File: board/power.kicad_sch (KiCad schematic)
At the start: 0 parts

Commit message: add: Hierarchical Sheets
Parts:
- added C10, C11: 100n, Capacitor_SMD:C_0603_1608Metric, symbol Device:C
- added C12, C13, C14, C15: 100pF, Capacitor_SMD:C_0201_0603Metric, symbol Device:C
- added J1: UART, Connector_PinSocket_2.54mm:PinSocket_1x02_P2.54mm_Vertical, symbol Connector_Generic:Conn_01x02
- added J2: USB_B, Connector_USB:USB_Mini-B_Lumberg_2486_01_Horizontal, symbol Connector:USB_B
- added U6: FT232RL, Package_SO:SSOP-28_5.3x10.2mm_P0.65mm, symbol Interface_USB:FT232RL
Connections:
- new net: J1.1 (Pin_1), U6.1 (TXD)
- new net: J1.2 (Pin_2), U6.5 (RXD)
- new net 5V: C10.1, C11.1, C12.1, C13.1, C14.1, C15.1, J2.1 (VBUS), U6.20 (VCC), U6.4 (VCCIO)
- new net ALARM: U6.19 (~{RESET})
- new net DT+: J2.3 (D+), U6.15 (USBD+)
- new net DT-: J2.2 (D-), U6.16 (USBD-)
- new net GND: C10.2, C11.2, C12.2, C13.2, C14.2, C15.2, J2.4 (GND), J2.5 (Shield), U6.18 (GND), U6.21 (GND), U6.25 (AGND), U6.26 (TEST), U6.7 (GND)
- no-connect marks 0 -> 14
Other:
- note added: "USB_P USB_N"
- note added: "desc: provide shortest return current path"
- note added: "entry source"
- note added: "exit sink"
- note added: "plane split"
- note added: "split boundary"

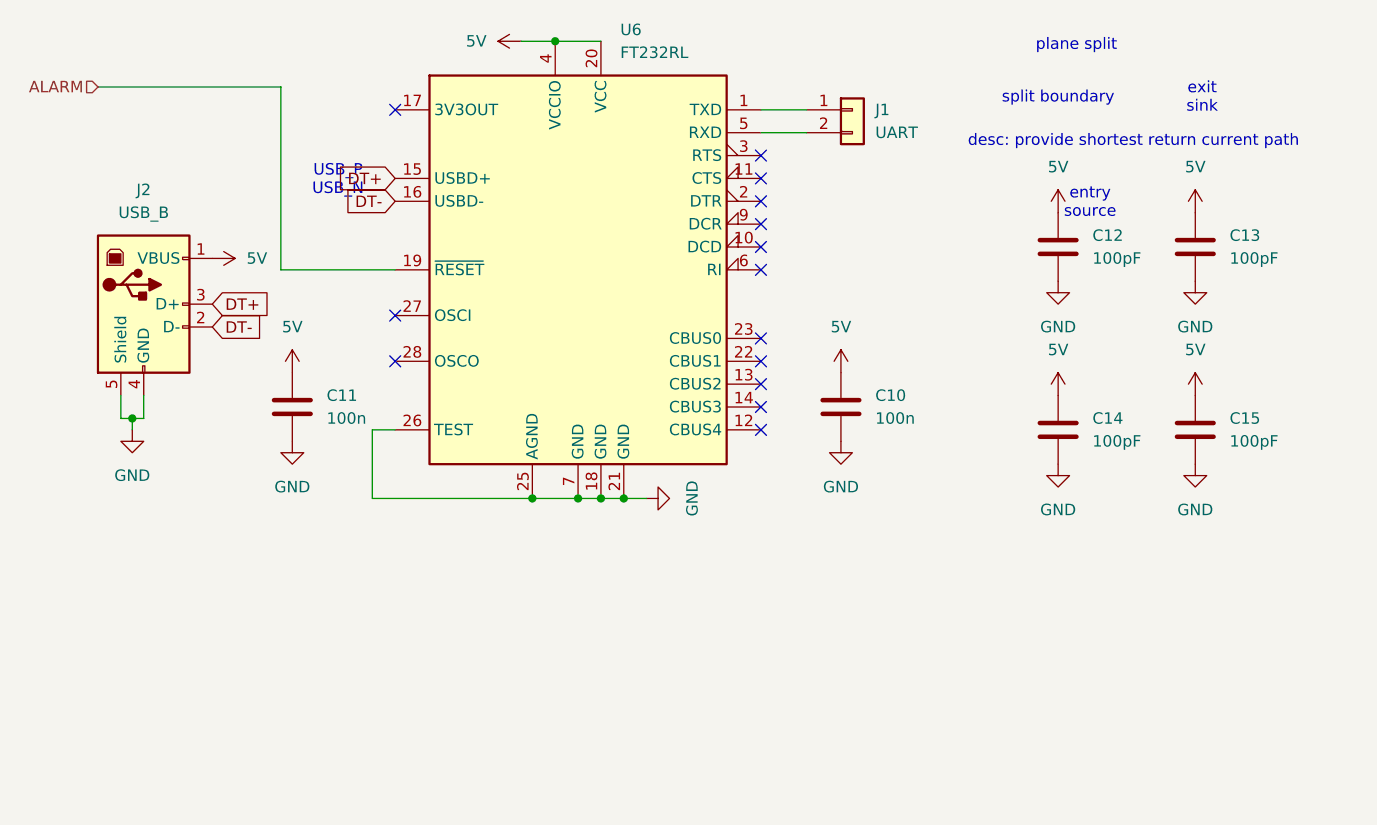
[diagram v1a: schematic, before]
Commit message: add: Mounting holes, box comments
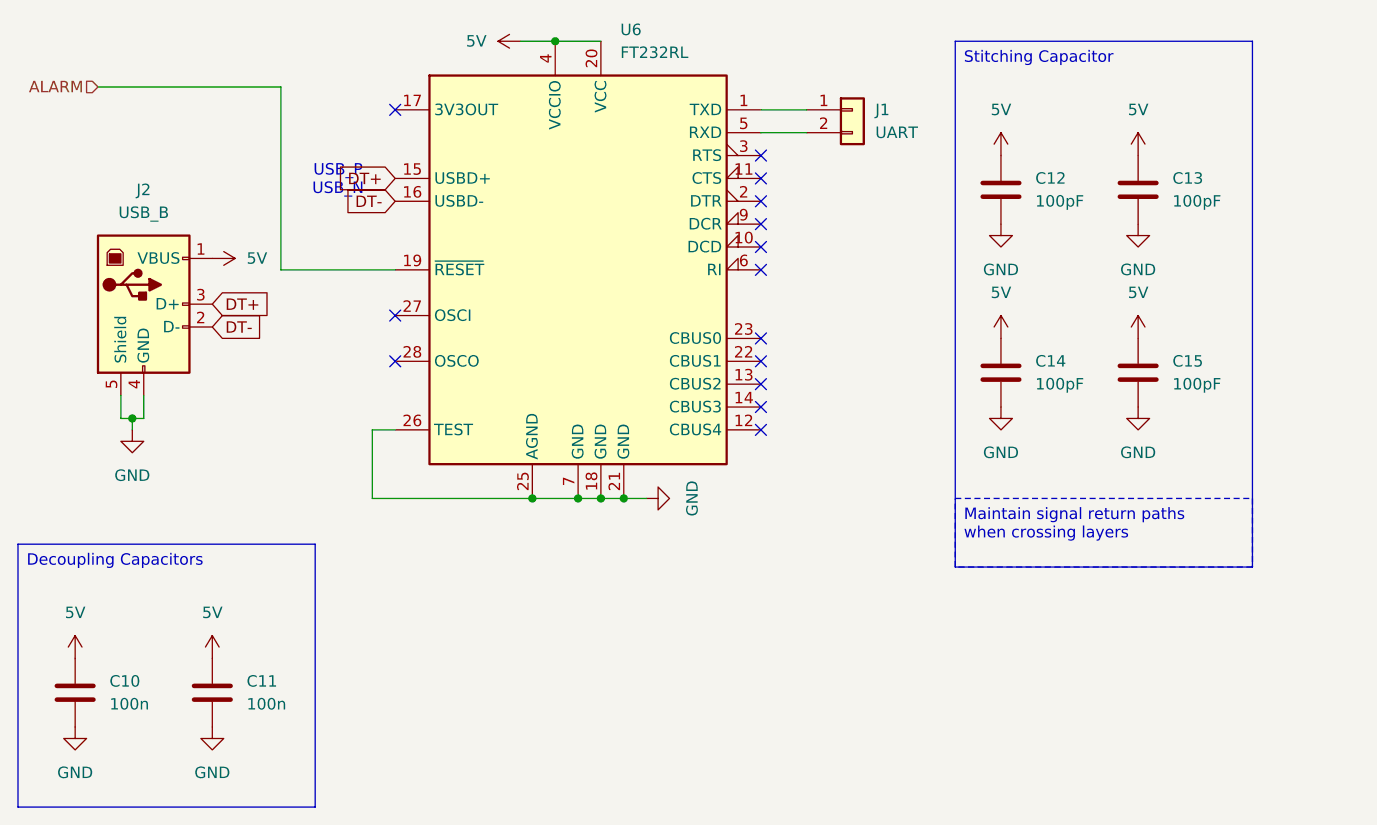
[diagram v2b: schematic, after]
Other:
- note removed: "desc: provide shortest return current path"
- note removed: "entry source"
- note removed: "exit sink"
- note removed: "plane split"
- note removed: "split boundary"
- moved on the sheet: C10, C11, C12, C13, C14, C15

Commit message: add: pcb layout & gerbers
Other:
- note removed: "USB_P USB_N"
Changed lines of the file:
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@@
 	(generator_version "9.0")
 	(paper "User" 177.8 127)
-	(text "USB_P\nUSB_N"
-		(exclude_from_sim no)
-		(at 54.61 35.814 0)
-		(effects
-			(font
-				(size 1.27 1.27)
-			)
-		)
-	)
 	(text_box "Stitching Capacitor"
 		(exclude_from_sim no)
@@
 	(wire
 		(pts
+			(xy 40.64 52.07) (xy 49.53 52.07)
+		)
+		(stroke
+			(width 0)
+			(type default)
+		)
+	)
+	(wire
+		(pts
 			(xy 48.26 45.72) (xy 48.26 25.4)
 		)
@@
 	(wire
 		(pts
+			(xy 40.64 49.53) (xy 49.53 49.53)
+		)
+		(stroke
+			(width 0)
+			(type default)
+		)
+	)
+	(wire
+		(pts
 			(xy 83.82 71.12) (xy 86.36 71.12)
 		)
@@
 		(pts
 			(xy 31.75 62.23) (xy 31.75 63.5)
+		)
+		(stroke
+			(width 0)
+			(type default)
+		)
+	)
+	(wire
+		(pts
+			(xy 57.15 35.56) (xy 60.96 35.56)
+		)
+		(stroke
+			(width 0)
+			(type default)
+		)
+	)
+	(wire
+		(pts
+			(xy 57.15 38.1) (xy 60.96 38.1)
 		)
 		(stroke
@@
 	(global_label "DT-"
 		(shape input)
-		(at 60.96 38.1 180)
+		(at 57.15 38.1 180)
 		(fields_autoplaced yes)
 		(effects
@@
 		)
 		(property "Intersheetrefs" "${INTERSHEET_REFS}"
-			(at 54.1648 38.1 0)
+			(at 50.3548 38.1 0)
 			(effects
 				(font
@@
 	(global_label "DT-"
 		(shape input)
-		(at 40.64 52.07 0)
+		(at 49.53 52.07 0)
 		(fields_autoplaced yes)
 		(effects
@@
 		)
 		(property "Intersheetrefs" "${INTERSHEET_REFS}"
-			(at 47.4352 52.07 0)
+			(at 56.3252 52.07 0)
 			(effects
 				(font
@@
 	(global_label "DT+"
 		(shape input)
-		(at 40.64 49.53 0)
+		(at 49.53 49.53 0)
 		(fields_autoplaced yes)
 		(effects
@@
 		)
 		(property "Intersheetrefs" "${INTERSHEET_REFS}"
-			(at 47.4352 49.53 0)
+			(at 56.3252 49.53 0)
 			(effects
 				(font
@@
 	(global_label "DT+"
 		(shape input)
-		(at 60.96 35.56 180)
+		(at 57.15 35.56 180)
 		(fields_autoplaced yes)
 		(effects
@@
 		)
 		(property "Intersheetrefs" "${INTERSHEET_REFS}"
-			(at 54.1648 35.56 0)
+			(at 50.3548 35.56 0)
 			(effects
 				(font
@@
 		(length 2.54)
 		(shape round)
-		(at 40.64 52.07 0)
-		(fields_autoplaced yes)
-		(effects
-			(font
-				(size 1.27 1.27)
-			)
-			(justify left bottom)
-		)
-		(property "Netclass" "Vias"
-			(at 41.3385 49.53 0)
+		(at 43.18 52.07 180)
+		(fields_autoplaced yes)
+		(effects
+			(font
+				(size 1.27 1.27)
+			)
+			(justify right bottom)
+		)
+		(property "Netclass" "USB"
+			(at 43.8785 54.61 0)
 			(effects
 				(font
@@
 		)
 		(property "Component Class" ""
-			(at -132.08 -59.69 0)
+			(at -129.54 -59.69 0)
 			(effects
 				(font
@@
 		(length 2.54)
 		(shape round)
-		(at 40.64 49.53 0)
+		(at 43.18 49.53 0)
 		(fields_autoplaced yes)
 		(effects
@@
 			(justify left bottom)
 		)
-		(property "Netclass" "Vias"
-			(at 41.3385 46.99 0)
+		(property "Netclass" "USB"
+			(at 43.8785 46.99 0)
 			(effects
 				(font
@@
 		)
 		(property "Component Class" ""
-			(at -132.08 -62.23 0)
-			(effects
-				(font
+			(at -129.54 -62.23 0)
+			(effects
+				(font
